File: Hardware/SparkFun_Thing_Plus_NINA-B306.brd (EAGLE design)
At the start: 22.9 x 66 mm, 84 parts, among them J1 USB-C, J2 THING_PLUS_LOGICAL, J3 CONN_03X2, J4 MICRO-SDFRICTION, J6 QWIIC_RA, Q1 20V/4.2A/52mΩ/1.4W, Q2 220mA/50V/3.5Ω, Q3 20V/4.2A/52mΩ/1.4W, U1 ESD Diode, U2 U-BLOX_NINA_B306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

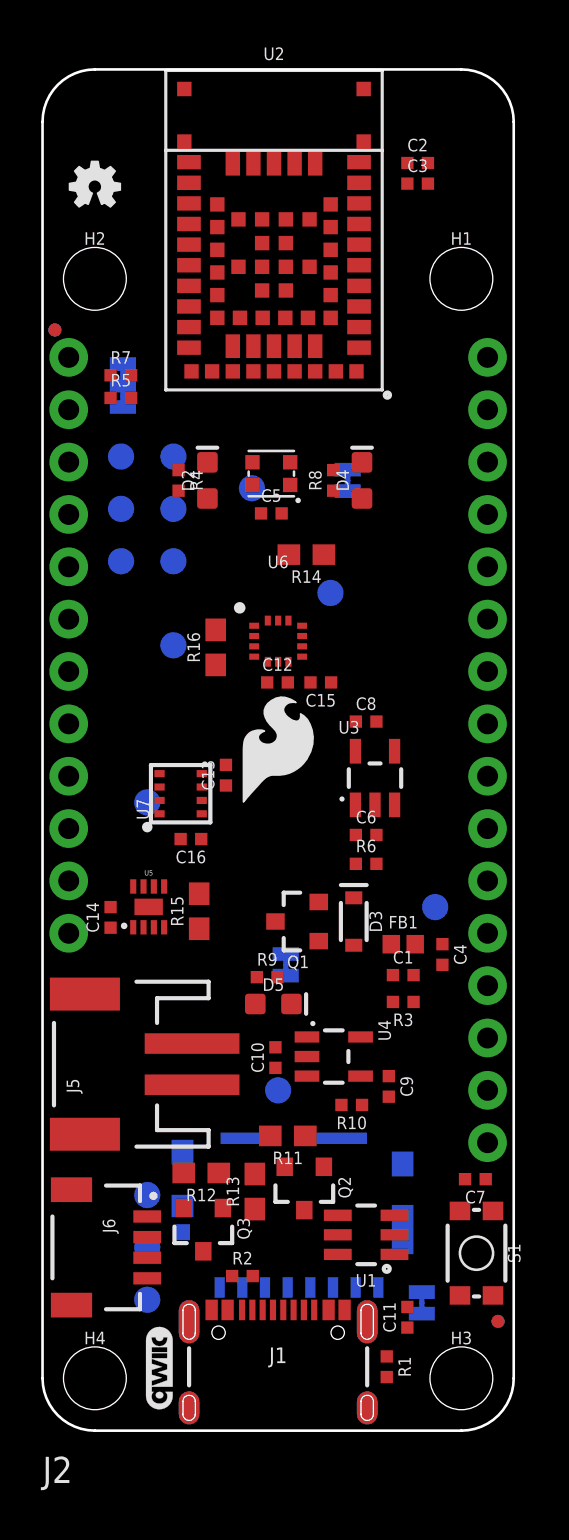
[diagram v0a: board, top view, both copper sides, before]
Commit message: Updates in prep for sch review
Schematic: Replaced 0603 10ks with 0402T package.

Board: Initial layout of parts complete.
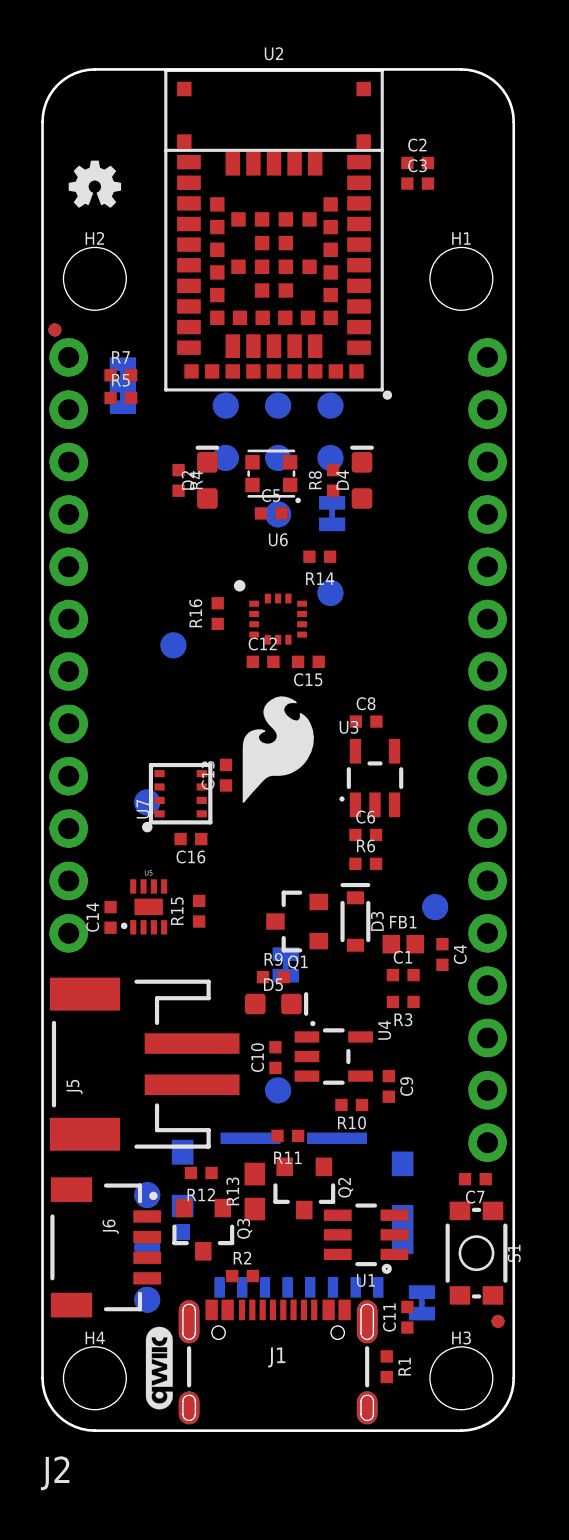
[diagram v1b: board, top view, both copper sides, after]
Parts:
- R11, R12, R14, R15, R16: device SparkFun-Resistors:0603 -> SparkFun-Resistors:0402-TIGHT
- moved J3 7.37 mm to (11.4, 48.5), turned to 180 degrees
- moved TP2 1.80 mm to (11.4, 44.5)
- moved PWR 1.78 mm to (14.1, 44.5)
- moved R16 1.64 mm to (8.50, 39.6)
- moved C12 1.22 mm to (10.7, 37.3)
- moved C15 1.17 mm to (12.9, 37.3)
- moved U6 1.07 mm to (11.4, 39.4)
- moved R14 0.66 mm to (13.4, 42.4)
- moved R9 0.30 mm to (11.2, 22.0)
- moved D3 0.08 mm to (15.2, 24.7)

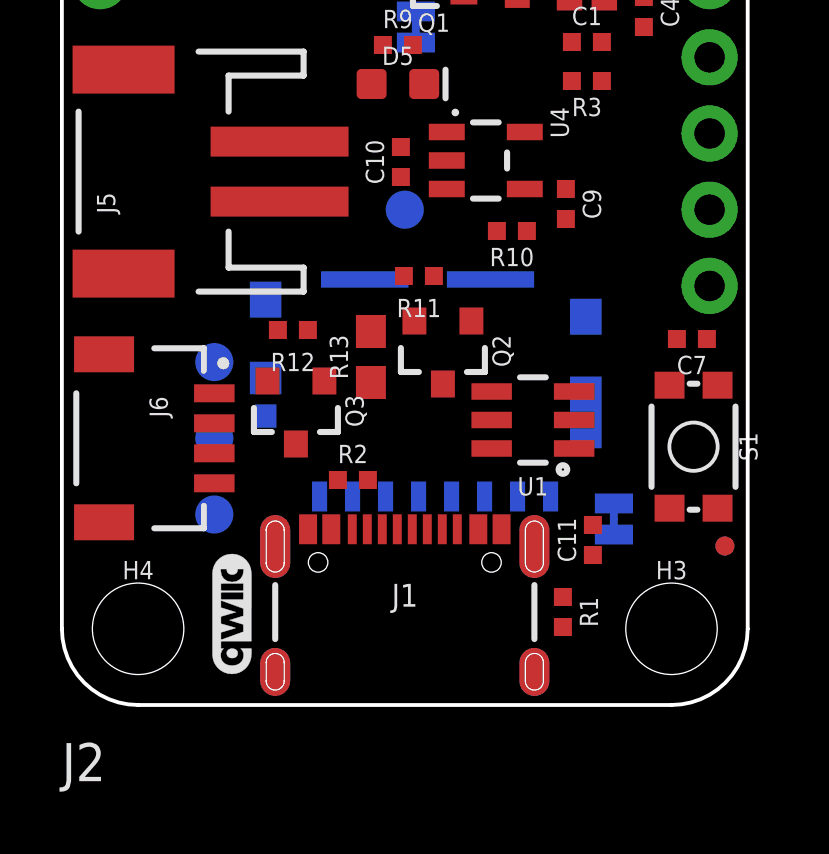
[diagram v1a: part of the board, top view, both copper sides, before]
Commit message: Changed package of 100R, rearrange board.
Changed 100R from 0603 to 0402T and rearranged the board to better organize that circuit. Also moved the QWIIC logo next to the QWIIC connector with the new space.
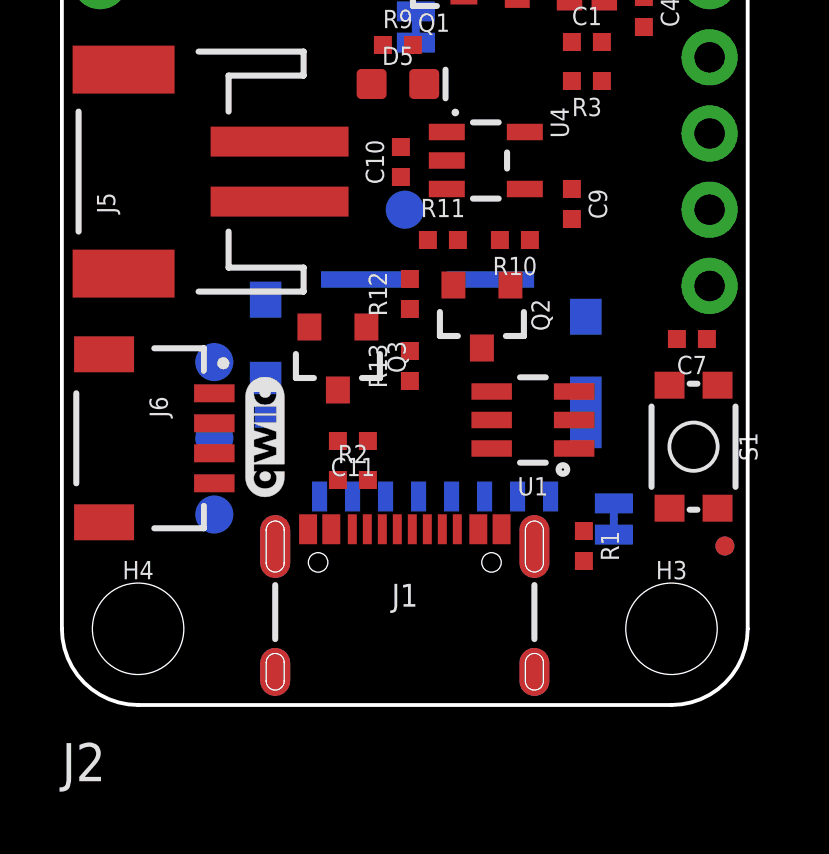
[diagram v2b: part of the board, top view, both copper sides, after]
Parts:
- R13: device SparkFun-Resistors:0603 -> SparkFun-Resistors:0402-TIGHT
- moved C11 8.65 mm to (9.70, 8.80), turned to 180 degrees
- moved LOGO4 6.00 mm to (6.78, 8.94)
- moved R12 4.08 mm to (11.6, 13.7), turned to 90 degrees
- moved R1 2.31 mm to (17.4, 5.30)
- moved Q3 2.28 mm to (9.20, 11.6)
- moved Q2 1.77 mm to (14.0, 13.0)
- moved R11 1.44 mm to (12.7, 15.5), turned to 0 degrees
- moved R13 1.33 mm to (11.6, 11.3)
- moved R10 0.32 mm to (15.1, 15.5)
- moved C9 0.20 mm to (17.0, 16.7)

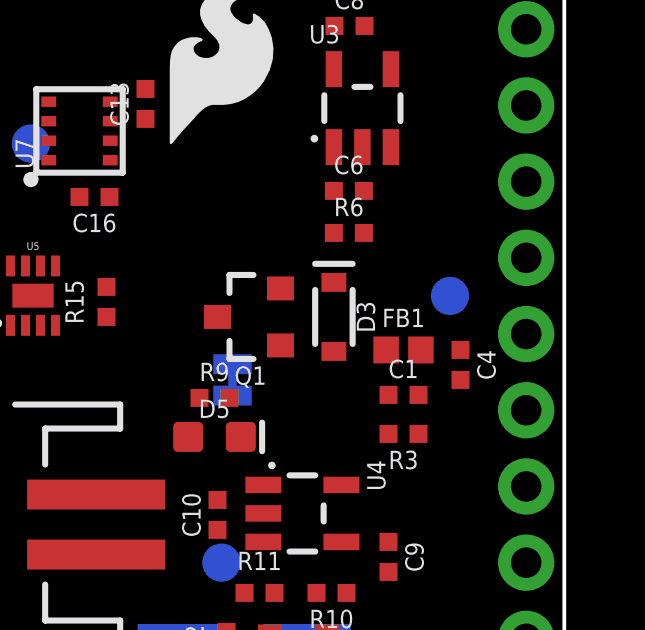
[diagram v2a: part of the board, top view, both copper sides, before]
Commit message: Added net classing, net names.
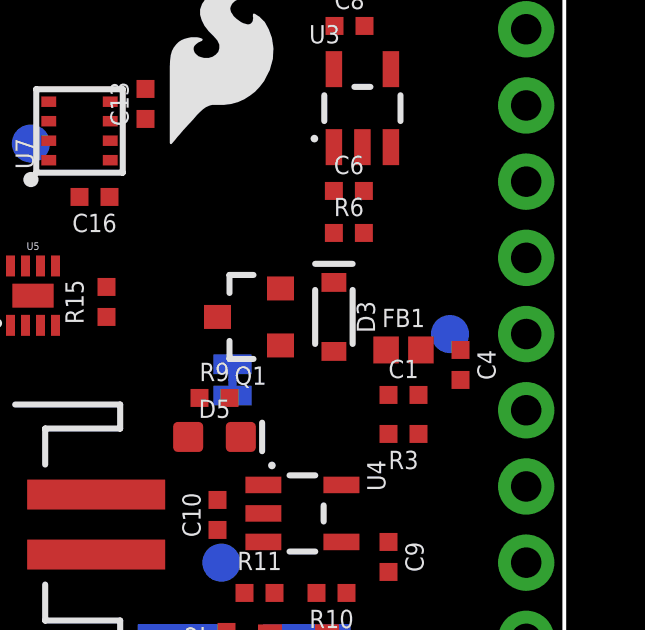
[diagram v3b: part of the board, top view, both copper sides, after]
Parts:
- moved TP1 1.27 mm to (19.1, 24.1)
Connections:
- net N$17 renamed SCL_PU_PWR
- net N$7 renamed 3V3_QWIIC
- net N$9 renamed SDA_PU_PWR
